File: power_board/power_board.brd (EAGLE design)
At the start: 63 x 70 mm, 33 parts, among them J5 20021311-00010T4LF, J6 20021311-00010T4LF, J7 20021311-00010T4LF, Q2 NPN, Q3 600mA/40V, Q4 NTMD4184PFR2G, U1 DRV8871, U11 INA219AIDCNR

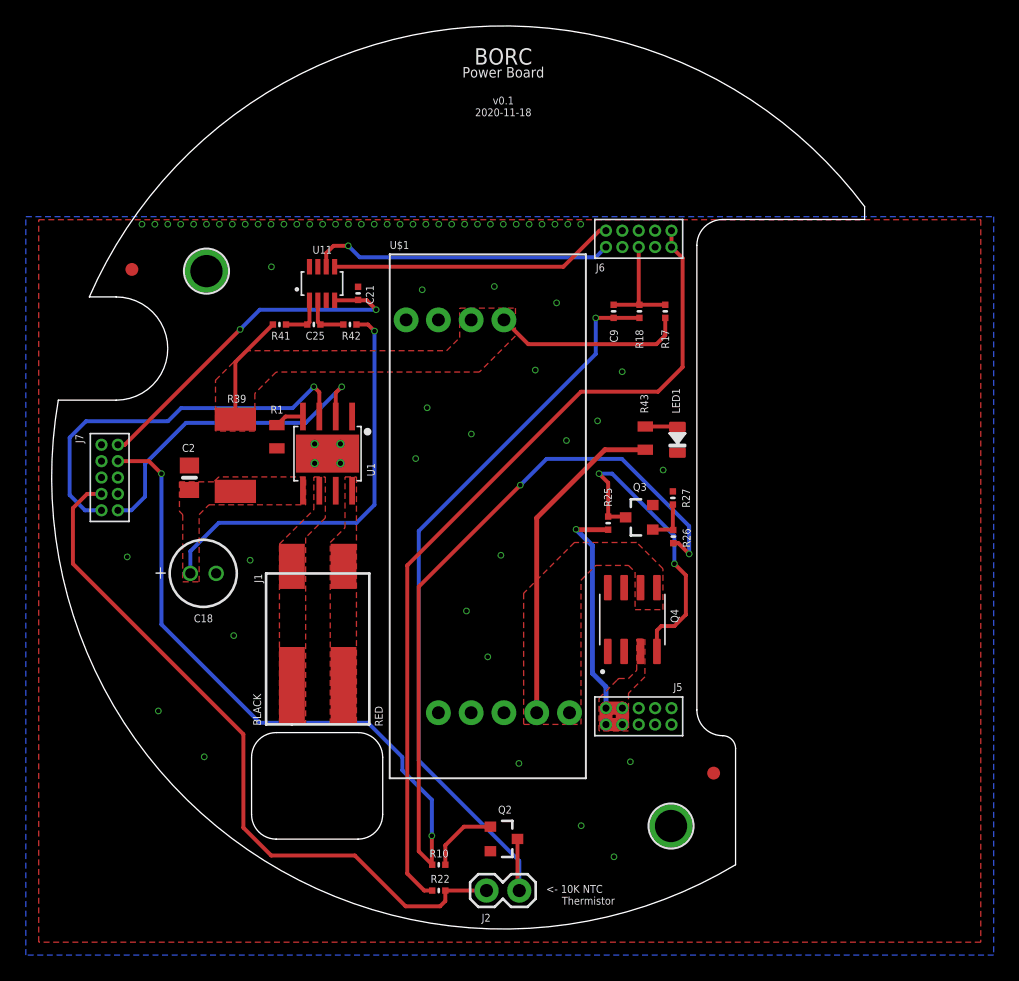
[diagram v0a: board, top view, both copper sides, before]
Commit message: Added 3D models for power board
- All components now have proper 3D models added to it
- Full 3D step file of the board now available (also in Fusion360)
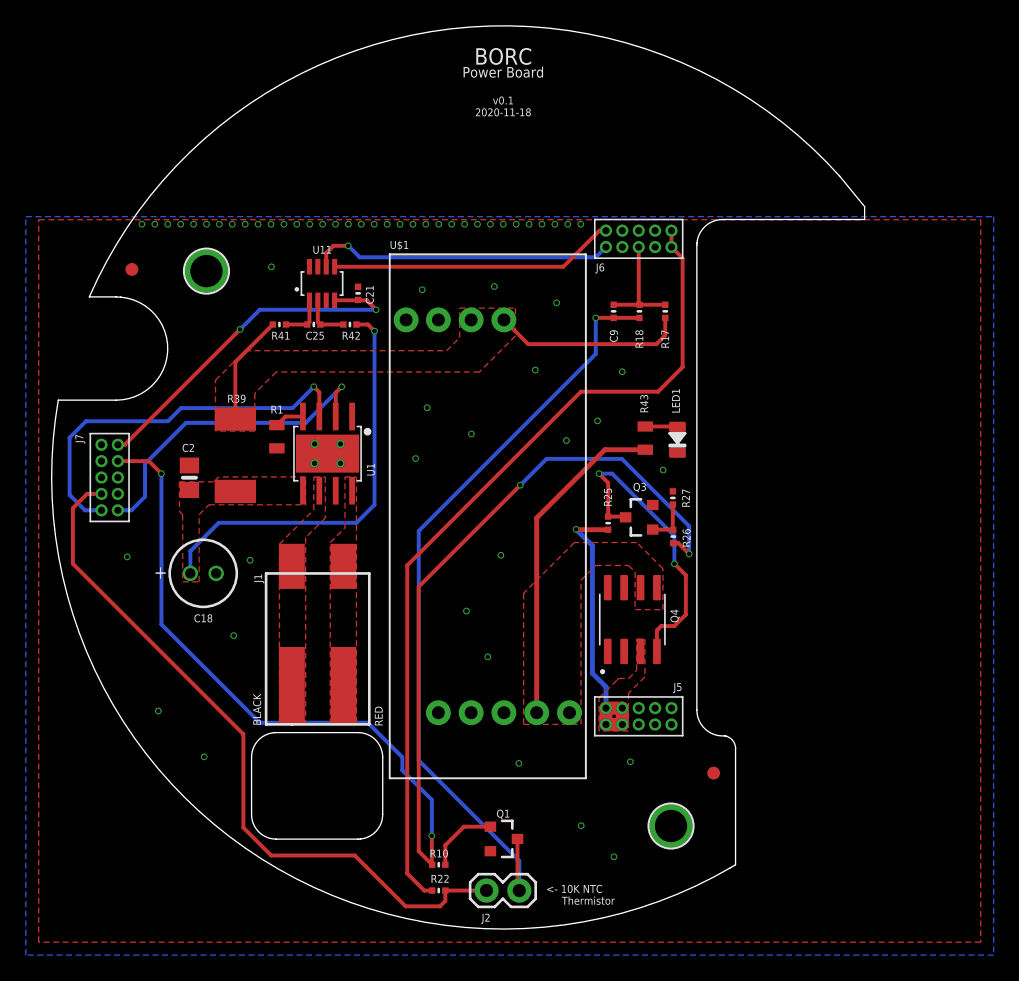
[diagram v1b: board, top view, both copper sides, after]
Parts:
- removed Q2: NPN, SparkFun-DiscreteSemi:SOT23-3@1
- added Q1: 600mA/40V, SparkFun-DiscreteSemi:SOT23-3
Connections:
- net GND: now also Q1.2; no longer Q2.2
- net GND0: now also Q1.3; no longer Q2.3
- net N$7: now also Q1.1; no longer Q2.1
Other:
- outline, holes or cut-outs redrawn

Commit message: v0.2 - power board update
- replaced DRV8871 driver with PCA9685 driver
- added more caps
- replaced 2-pin poke home with 3-pin 2.54mm header
- rerouted many traces and vias
- moved some components around
- added schematic
- updated render, gerber
- ERC/DRC
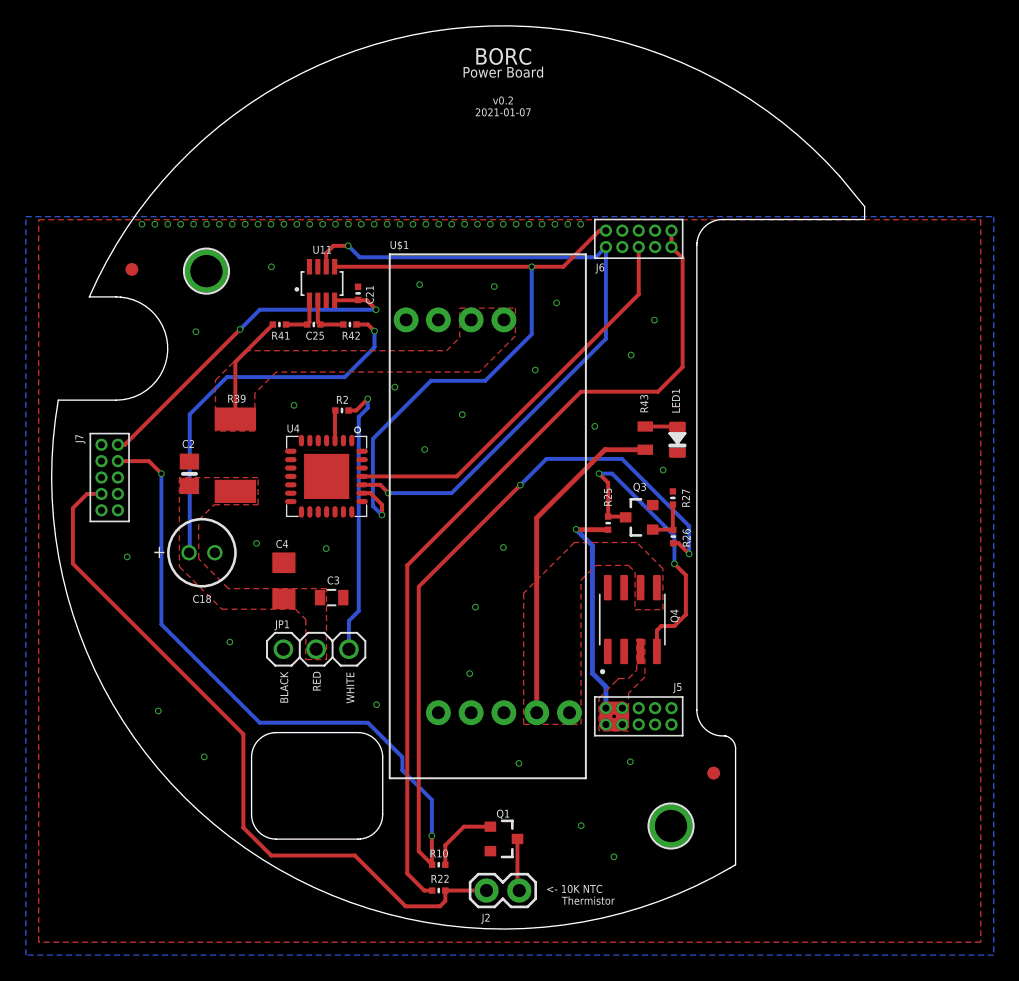
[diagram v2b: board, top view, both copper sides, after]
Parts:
- removed C9: 0.1uF, Adafruit Feather 32u4 Bluefruit LE:MICROBUILDER__0402MP
- removed J1: (no value), SparkFun-Connectors:1X02_POKEHOME
- removed R1: 30K, SparkFun-Resistors:0805
- removed R17: 47.5K, Adafruit Feather 32u4 Bluefruit LE:MICROBUILDER__0402MP
- removed R18: 10K, Adafruit Feather 32u4 Bluefruit LE:MICROBUILDER__0402MP
- removed U1: DRV8871, microbuilder:HSOP8
- added C3: 10uF, SparkFun-Passives:0805
- added C4: 2.2uF, SparkFun-Passives:1206
- added JP1: (no value), adafruit:1X03
- added R2: 220, Adafruit Feather 32u4 Bluefruit LE:MICROBUILDER__0402MP
- added U4: (no value), PCA9685:HVQFN28_SOT788-1
- moved C18 1.60 mm to (11.6, 29.2)
- moved C2 0.30 mm to (10.7, 35.3)
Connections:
- removed net 12V: R17.2, R39.2, R41.1, U$1.VOUT@1, U$1.VOUT@2
- removed net 12V_POWER: C18.1, C2.1, R39.1, R42.1, U1.5
- removed net 12V_SENSE: C9.1, J6.5, R17.1, R18.1
- removed net N$2: R1.2, U1.4
- removed net OUT1: J1.P1, J1.P3, U1.6
- removed net OUT2: J1.P2, J1.P4, U1.8
- new net 5V: R39.2, R41.1, U$1.VOUT@1, U$1.VOUT@2
- new net 5V_POWER: C18.1, C2.1, C3.1, C4.1, JP1.2, R39.1, R42.1
- new net CH0: JP1.3, R2.1
- new net DRIVER_CONTROL: J6.5, U4.25
- new net N$9: R2.2, U4.3
- net GND: now also C3.2, C4.2, JP1.1, U4.11, U4.20, U4.22, U4.TH; no longer R1.1, U1.1, U1.7, U1.GND, U1.P$1, U1.P$2, U1.P$3, U1.P$4
- net GND0: no longer C9.2, R18.2
- net IN1: no longer U1.3
- net IN2: no longer U1.2
- net SCL: now also U4.23
- net SDA: now also U4.24
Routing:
- net GND0: track 60.7 -> 4.06 mm, vias 1 -> 0
- net 12V_POWER: track 32.5 -> 0.00 mm, vias 1 -> 0
- net SDA: track 23.7 -> 54.9 mm, vias 1 -> 2
- net DRIVER_CONTROL: track 0.00 -> 30.9 mm
- net IN1: track 30.4 -> 0.00 mm, vias 1 -> 0
- net 5V_POWER: track 0.00 -> 30.1 mm, vias 0 -> 1
- net SCL: track 22.2 -> 52.0 mm, vias 0 -> 2
- net IN2: track 25.3 -> 0.00 mm, vias 1 -> 0
- net 12V: track 23.5 -> 0.00 mm
- net CH0: track 0.00 -> 21.9 mm, vias 0 -> 1
- net 5V: track 0.00 -> 8.54 mm
- net 12V_SENSE: track 8.50 -> 0.00 mm
- net N$9: track 0.00 -> 2.35 mm
- net N$2: track 2.29 -> 0.00 mm
- added copper zone on layer 1, net 5V
- added copper zone on layer 1, net 5V_POWER
- removed copper zone on layer 1, net 12V
- removed copper zone on layer 1, net 12V_POWER
- removed copper zone on layer 1, net OUT1
- removed copper zone on layer 1, net OUT2
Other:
- board text added: "WHITE"
- board text added: "v0.2 2021-01-07"
- board text removed: "v0.1 2020-11-18"

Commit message: v0.3 - power board update
- design update
- replaced U3V70x with U1V11x step up voltage regulator. This steps up from batt. voltage (~4V) to 5V from as low as 0.5V. This allows servo to work even with large voltage drops
- Added extra caps on input and output of voltage reg.
- Increased cutout for servo cable to go outside the board dimension. Allows more room for wire to bend
- pushed servo cable header pins further in the board to allow room for large connector head
- moved traces and components around to accomodate new design
- silkscreen, dimensions, board outline (dxf), gerbers, render & schematic update
- 3D step file still not updated
- ERC/DRC
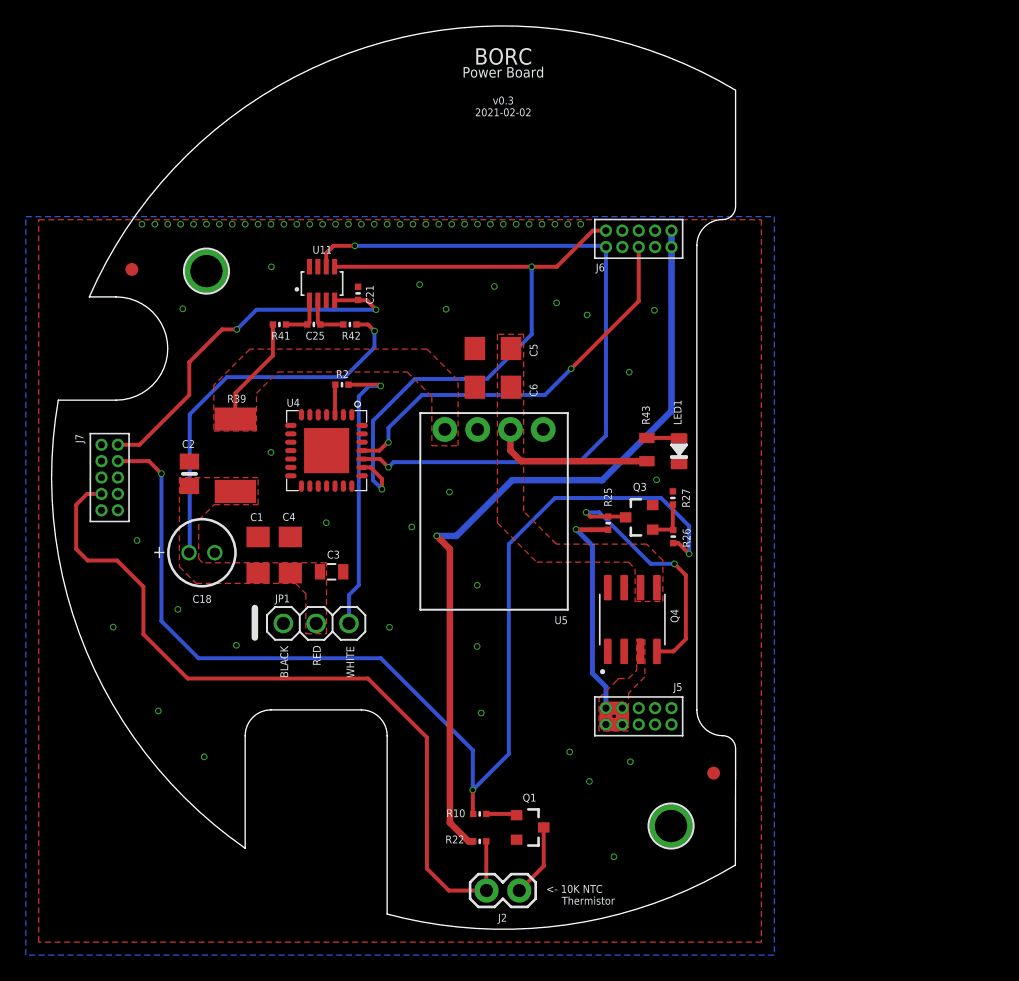
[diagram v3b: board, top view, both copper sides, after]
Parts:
- removed U$1: POLOLU_12V_STEPUP_U3V70F12, Pololu U3V70x Step Up:POLOLU_12V_STEPUP_U3V70F12
- added C1: 2.2uF, SparkFun-Passives:1206
- added C5, C6: 10uF, SparkFun-Passives:1206
- added U5: POLOLU_STEPUP_U1V11X, Pololu Step Up Vregs:POLOLU_STEPUP_U1V11X
- moved R10 5.06 mm to (33.2, 8.94)
- moved R22 4.96 mm to (33.2, 6.81)
- moved Q1 2.22 mm to (37.0, 7.89)
- moved C4 2.06 mm to (18.5, 29.0)
- moved C3 2.00 mm to (21.7, 27.7)
- moved JP1 2.00 mm to (20.5, 23.7)
- moved R2 2.00 mm to (22.5, 42.2)
- moved U4 2.00 mm to (17.5, 40.9)
- moved R43 0.90 mm to (46.1, 37.2)
- moved LED1 0.90 mm to (48.6, 37.0)
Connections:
- removed net IN1: J7.1
- removed net IN2: J7.2
- net 5V: now also U5.VOUT; no longer U$1.VOUT@1, U$1.VOUT@2
- net 5V_POWER: now also C1.1
- net GND: now also C1.2, C5.2, C6.2, U5.GND; no longer U$1.GND@1, U$1.GND@2, U$1.GND@3, U$1.GND@4
- net VBAT_ON: now also C5.1, C6.1, U5.VIN; no longer U$1.VIN@1, U$1.VIN@2
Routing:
- net VBAT_ON: track 25.7 -> 12.6 mm
- net MOTOR_CONTROL: track 100.6 -> 88.7 mm, vias 4 -> 3
- net TEMP: track 55.3 -> 60.4 mm
- net VCC: track 65.0 -> 61.2 mm, vias 0 -> 1
- net N$7: track 5.60 -> 2.39 mm
- net N$32: track 23.7 -> 20.6 mm
- net SDA: track 54.9 -> 57.8 mm
- net GND0: track 4.06 -> 5.67 mm
- net CURRENT_SENSE_POWER: track 27.9 -> 29.4 mm
- net SCL: track 52.0 -> 50.8 mm
- net CH0: track 21.9 -> 22.5 mm
- net DRIVER_CONTROL: track 30.9 -> 31.1 mm, vias 0 -> 2
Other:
- board size 63 x 70 mm -> 53 x 70 mm
- board text added: "v0.3 2021-02-02"
- board text removed: "v0.2 2021-01-07"

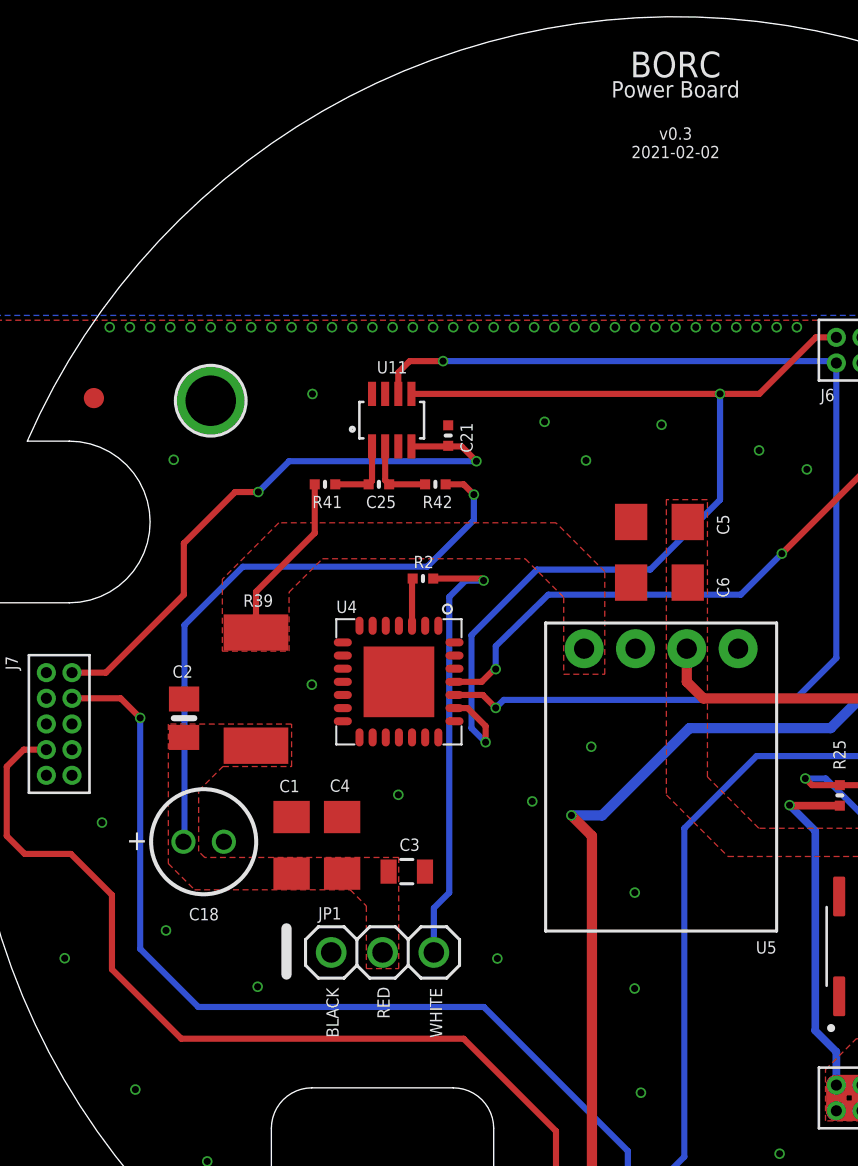
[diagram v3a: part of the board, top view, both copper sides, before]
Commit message: v0.4 - power board update
- INA219 I2C address now changed from 0x40 to 0x44 to avoid conflict with PCA9685 (added pull-up resistor on pin A0)
- gerber files updated
- everything else functionally the same
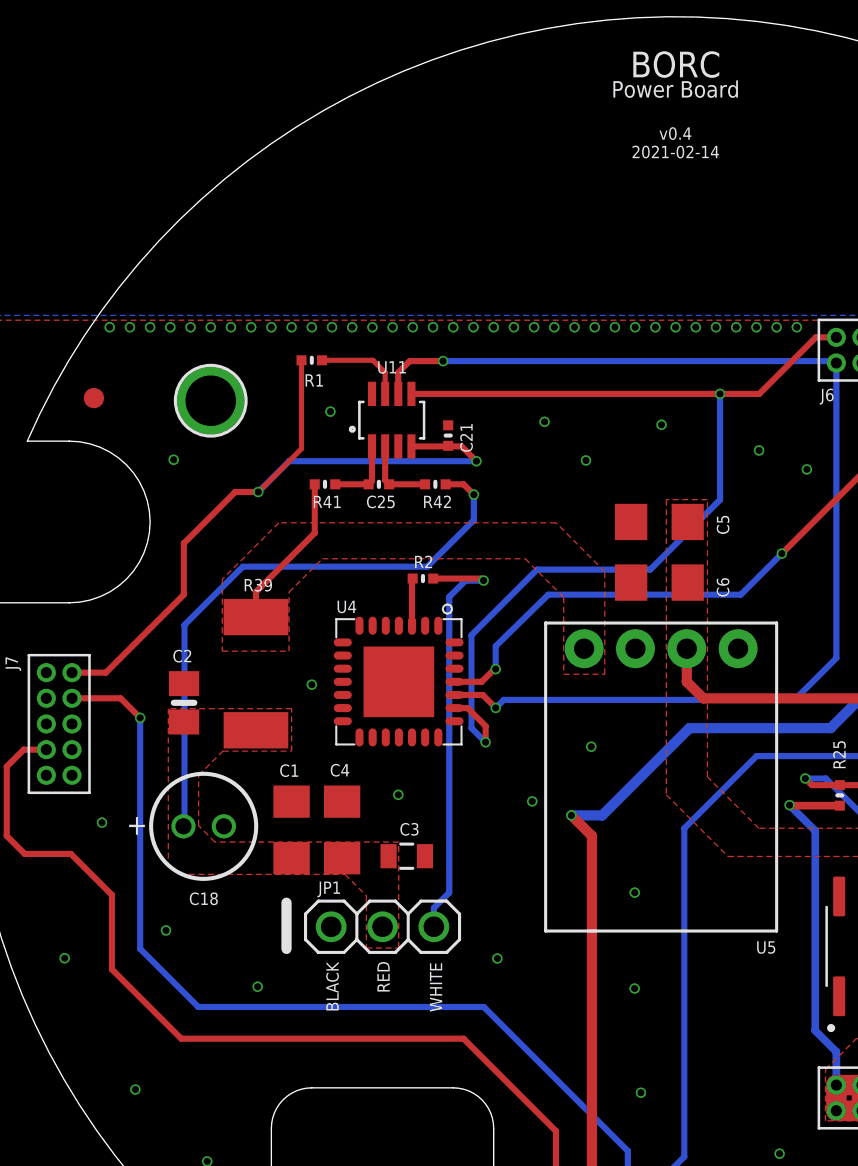
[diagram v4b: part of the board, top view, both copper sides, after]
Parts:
- added R1: 10K, Adafruit Feather 32u4 Bluefruit LE:MICROBUILDER__0402MP
- moved JP1 1.27 mm to (20.5, 25.0)
- moved C1 0.76 mm to (16.0, 29.8)
- moved C18 0.76 mm to (11.6, 29.9)
- moved C2 0.76 mm to (10.7, 36.1)
- moved C3 0.76 mm to (21.7, 28.5)
- moved C4 0.76 mm to (18.5, 29.8)
- moved R39 0.76 mm to (14.2, 37.5)
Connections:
- new net N$1: R1.2, U11.7
- net CURRENT_SENSE_POWER: now also R1.1
- net GND: no longer U11.7
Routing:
- net CURRENT_SENSE_POWER: track 29.4 -> 36.8 mm
- net N$1: track 0.00 -> 4.43 mm
- net CH0: track 22.5 -> 21.2 mm
- net 5V_POWER: track 30.1 -> 29.3 mm
- net 5V: track 8.54 -> 7.78 mm
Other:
- board text added: "v0.4 2021-02-14"
- board text removed: "v0.3 2021-02-02"
